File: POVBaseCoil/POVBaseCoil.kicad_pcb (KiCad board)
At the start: 2 copper layers, 68 x 81.2 mm, 10 parts, among them P1 CONN_01X05, P2 CONN_01X01, P3 CONN_01X01

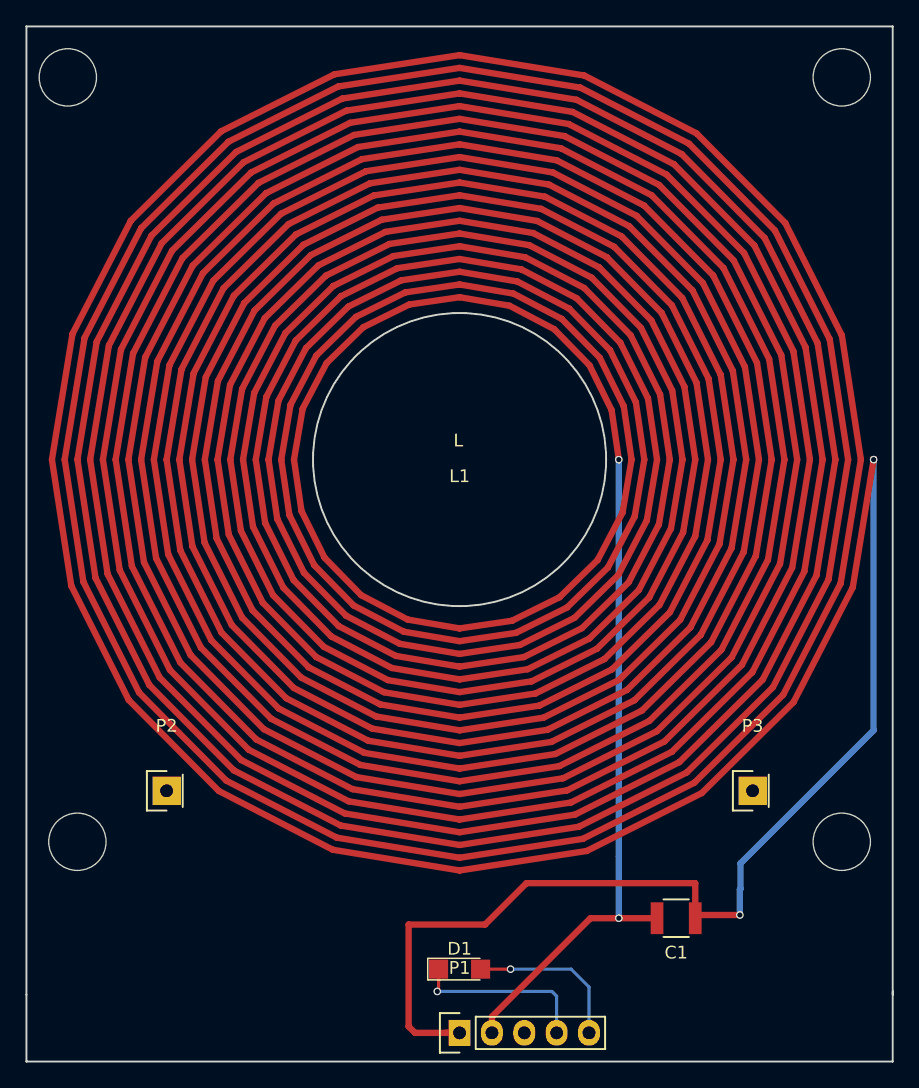
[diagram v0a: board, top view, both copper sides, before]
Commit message: Updated the designs with better cutouts and 3D parts.
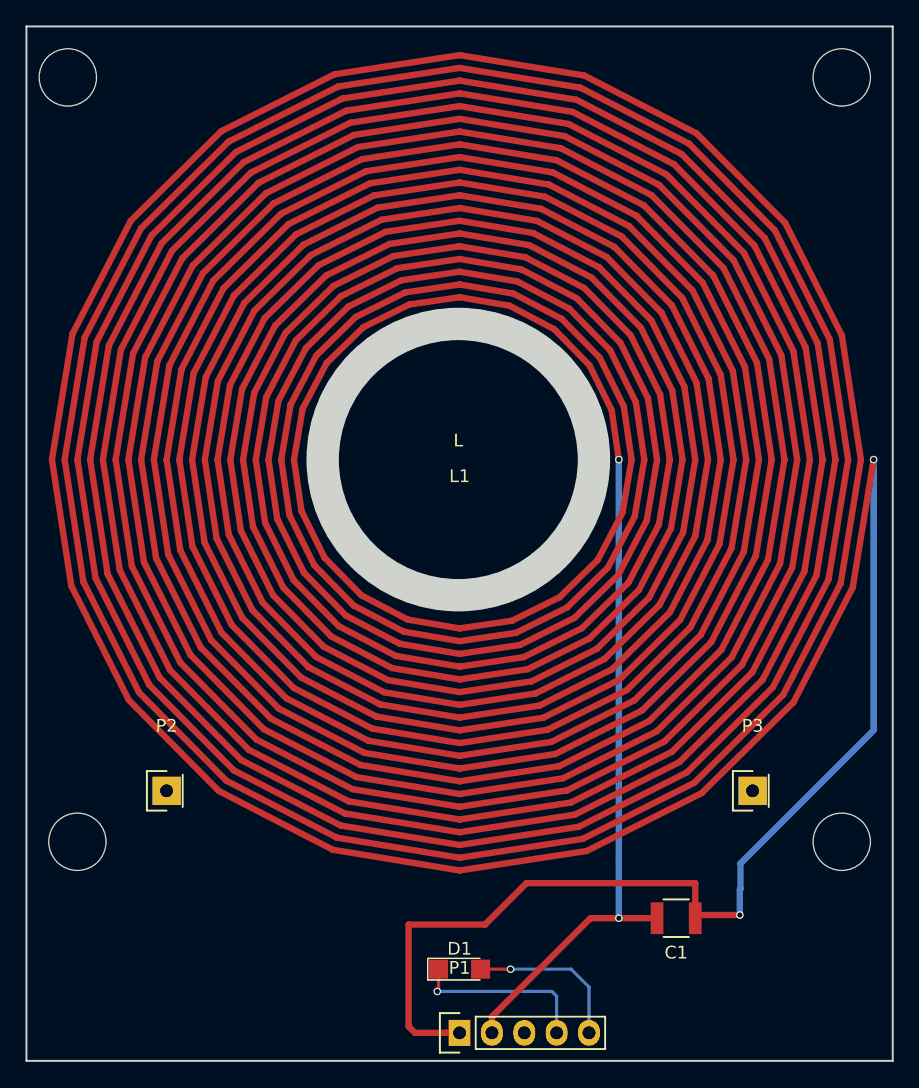
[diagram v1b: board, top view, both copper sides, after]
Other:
- outline, holes or cut-outs redrawn
